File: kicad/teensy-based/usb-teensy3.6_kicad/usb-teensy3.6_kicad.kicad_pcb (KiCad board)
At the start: 2 copper layers, 154.9 x 90.2 mm, 20 parts, among them SW1 SW_Push, SW2 SW_Push, U1 Teensy3.6

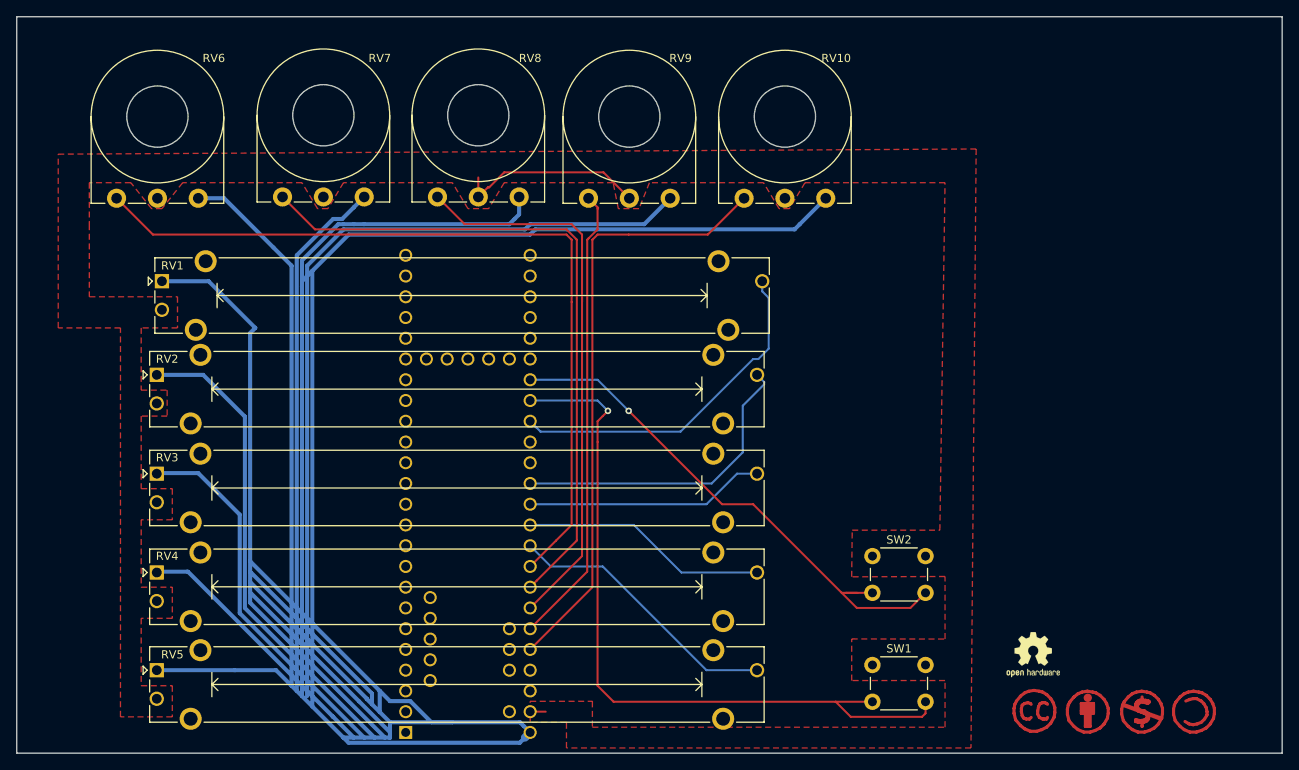
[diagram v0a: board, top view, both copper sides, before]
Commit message: modifies the soilmask and printing to underline the community thing a bit more
adds scheme to readme and howto order

As hint: I know you can easier order if the gerber files are already uploaded to a manufacturer, but as this is combine to the Affiliate Systems I decided not to.
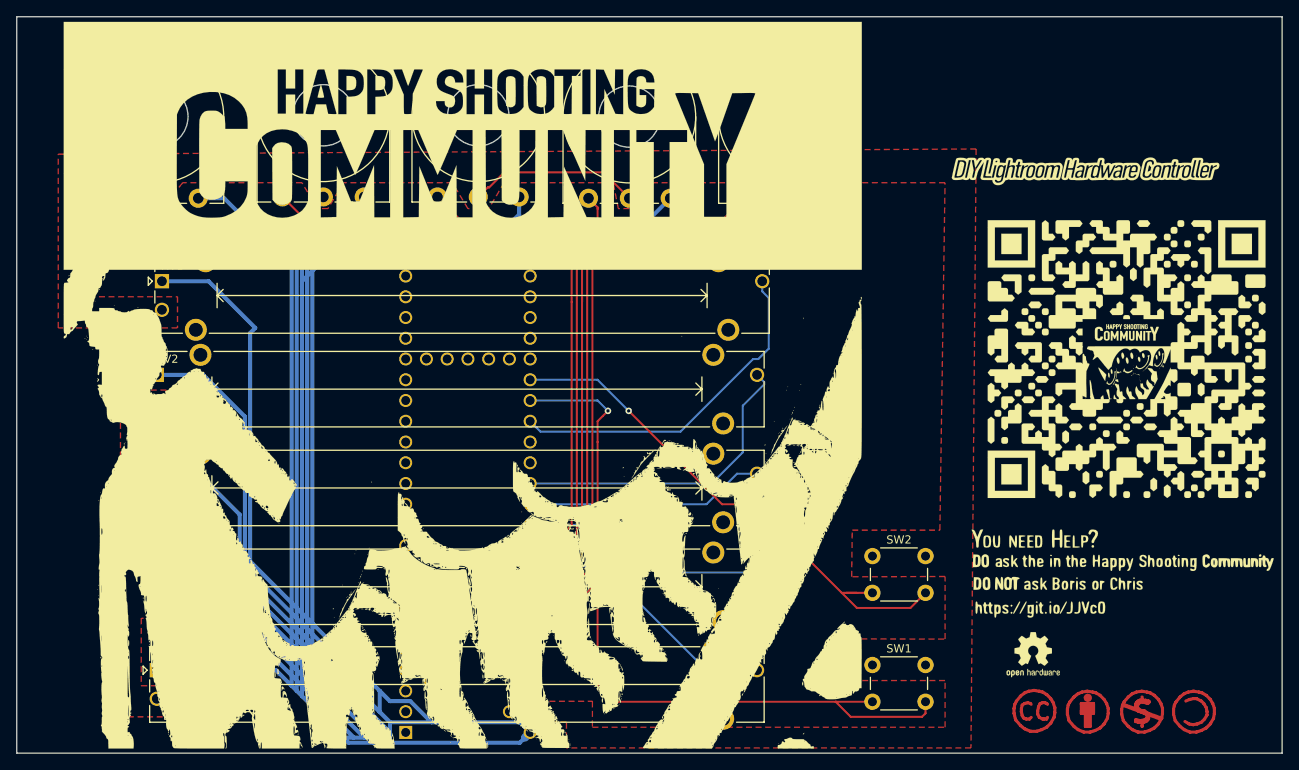
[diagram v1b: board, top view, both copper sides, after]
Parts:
- removed HSLogo: LOGO, HappyShooting:HSSilk_big
- removed HSLogoText: LOGO, HappyShooting:hsc_pcb_text_small
- added G***: LOGO, HappyShooting:hct_diff_print_i, F.Cu at (128.3, 104.8)
- added G***: LOGO, HappyShooting:diy_silk_i, F.Cu at (203.8, 78.1)
- added G***: LOGO, HappyShooting:diy_print, F.Cu at (203.8, 78.1)
- added G***: LOGO, HappyShooting:help_print, F.Cu at (209.6, 127.6)
- added G***: LOGO, HappyShooting:qr_medium, F.Cu at (209.6, 101.6)
- added G***: LOGO, HappyShooting:hct_silk_i, F.Cu at (128.3, 104.8)

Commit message: changed help wording on pcb and scheme
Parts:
- removed the G*** at (209.6, 127.6)
- added G***: LOGO, HappyShooting:help_print_350, F.Cu at (210.2, 127.6)
- moved G*** 0.64 mm to (127.6, 104.8)

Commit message: mod render without parts
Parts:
- removed the G*** at (128.3, 104.8)
- removed the G*** at (127.6, 104.8)
- removed RV1: 10k sl, Potentiometer_THT:Potentiometer_Bourns_PTA6043_Single_Slide
- added G***: LOGO, HappyShooting:hsc_diff_print_i_375, F.Cu at (130.8, 104.8)
- added G***: LOGO, HappyShooting:hsc_silk_375, F.Cu at (130.8, 104.8)

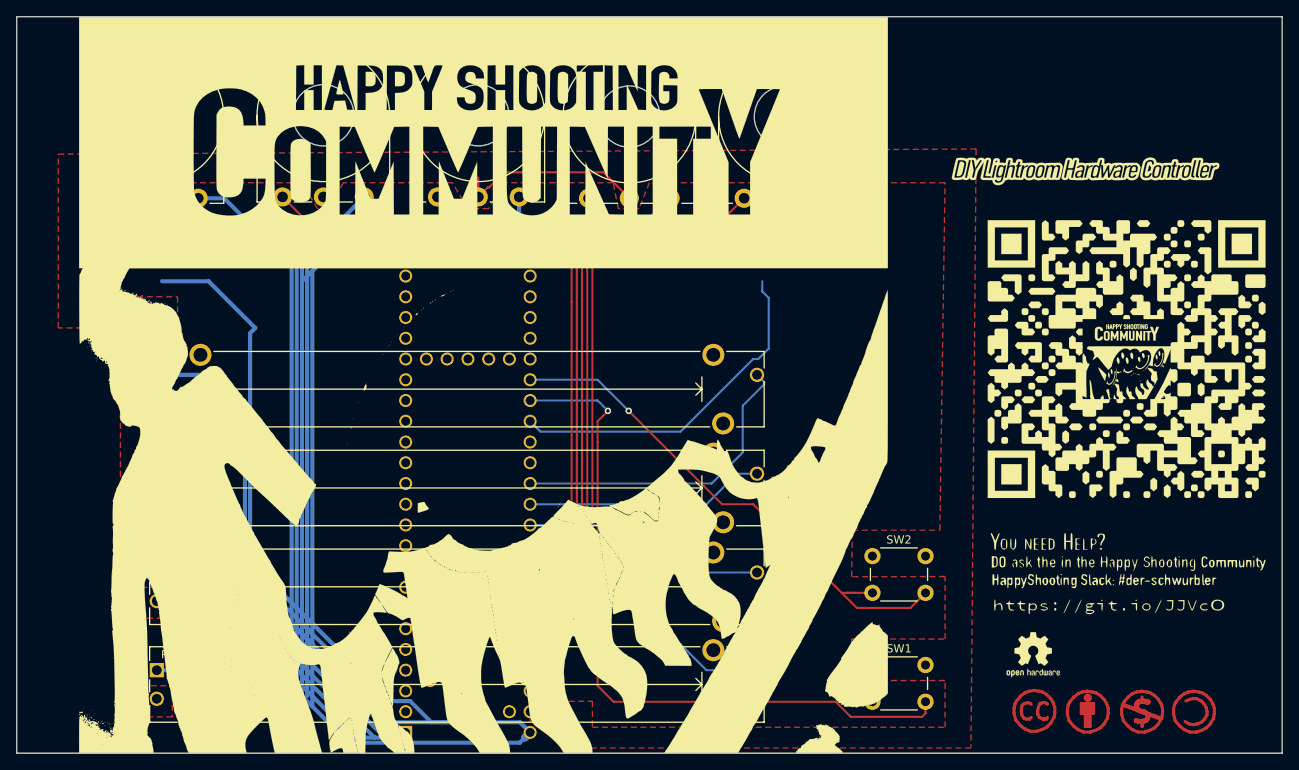
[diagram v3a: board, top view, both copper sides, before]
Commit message: update pcb with alternative layout
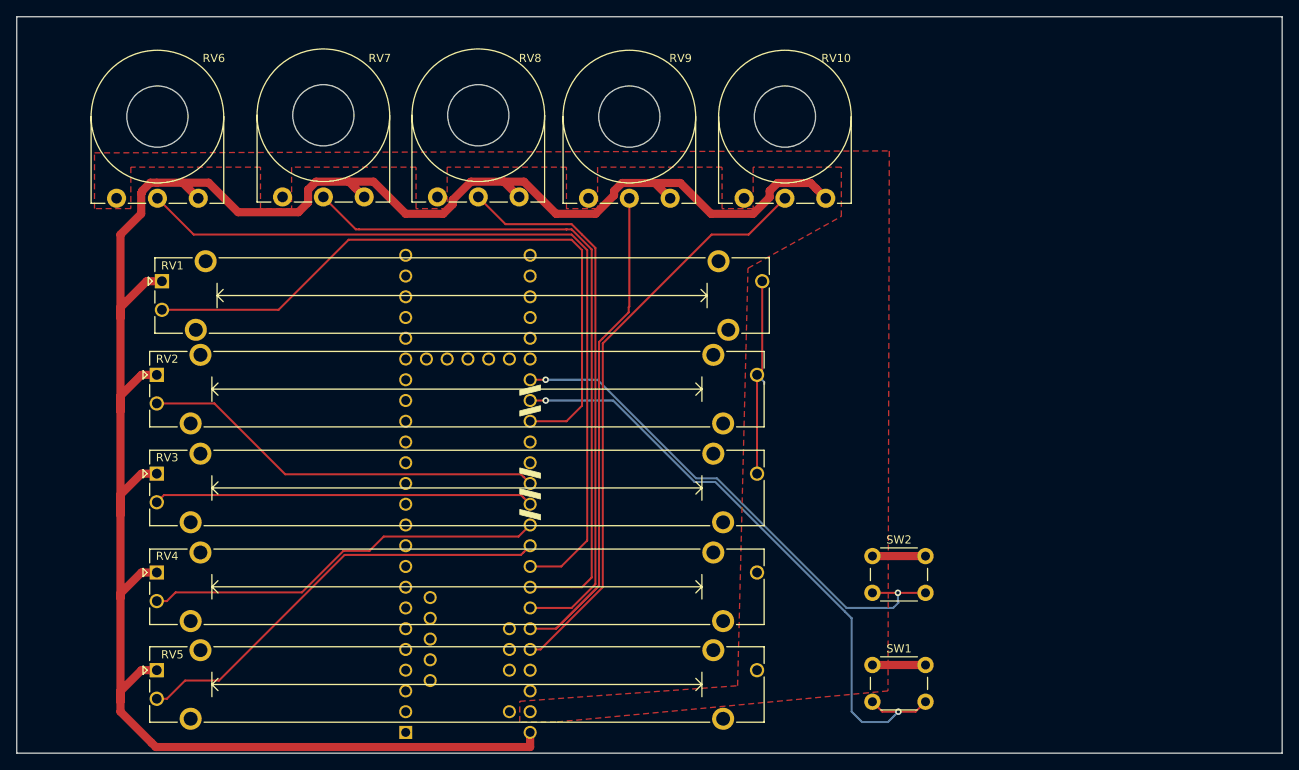
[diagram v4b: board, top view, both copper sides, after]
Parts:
- removed G***: LOGO, HappyShooting:hsc_diff_print_i_375
- removed G***: LOGO, HappyShooting:hsc_silk_375
- removed G***: LOGO, HappyShooting:help_print_350
- removed G***: LOGO, HappyShooting:diy_silk_i
- removed G***: LOGO, HappyShooting:diy_print
- removed G***: LOGO, HappyShooting:qr_medium
- removed REF**: Symbol_CC-ShareAlike_CopperTop_Small, Symbol:Symbol_CC-ShareAlike_CopperTop_Small
- removed REF**: Symbol_CreativeCommons_CopperTop_Type2_Small, Symbol:Symbol_CreativeCommons_CopperTop_Type2_Small
- removed REF**: OSHW-Logo2_7.3x6mm_SilkScreen, Symbol:OSHW-Logo2_7.3x6mm_SilkScreen
- removed REF**: Symbol_CC-Attribution_CopperTop_Small, Symbol:Symbol_CC-Attribution_CopperTop_Small
- removed REF**: Symbol_CC-Noncommercial_CopperTop_Small, Symbol:Symbol_CC-Noncommercial_CopperTop_Small
- added RV1: 10k sl, Potentiometer_THT:Potentiometer_Bourns_PTA6043_Single_Slide, F.Cu at (91.4, 92.1)
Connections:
- RV10 pad 2: GND -> Net-(RV10-Pad2)
- RV10 pad 3: Net-(RV10-Pad3) -> GND
- RV2 pad 2: GND -> Net-(RV2-Pad2)
- RV2 pad 3: Net-(RV2-Pad3) -> GND
- RV3 pad 2: GND -> Net-(RV3-Pad2)
- RV3 pad 3: Net-(RV3-Pad3) -> GND
- RV4 pad 2: GND -> Net-(RV4-Pad2)
- RV4 pad 3: Net-(RV4-Pad3) -> GND
- RV5 pad 2: GND -> Net-(RV5-Pad2)
- RV5 pad 3: Net-(RV5-Pad3) -> GND
- RV6 pad 2: GND -> Net-(RV6-Pad2)
- RV6 pad 3: Net-(RV6-Pad3) -> GND
- RV7 pad 2: GND -> Net-(RV7-Pad2)
- RV7 pad 3: Net-(RV7-Pad3) -> GND
- RV8 pad 2: GND -> Net-(RV8-Pad2)
- RV8 pad 3: Net-(RV8-Pad3) -> GND
- RV9 pad 2: GND -> Net-(RV9-Pad2)
- RV9 pad 3: Net-(RV9-Pad3) -> GND
- U1 pad 41: Net-(RV2-Pad3) -> Net-(RV2-Pad2)
- U1 pad 42: Net-(RV3-Pad3) -> Net-(RV3-Pad2)
- U1 pad 43: Net-(RV4-Pad3) -> Net-(RV4-Pad2)
- U1 pad 44: Net-(RV5-Pad3) -> Net-(RV5-Pad2)
- U1 pad 45: Net-(RV6-Pad3) -> Net-(RV6-Pad2)
- U1 pad 46: Net-(RV7-Pad3) -> Net-(RV7-Pad2)
- U1 pad 47: Net-(RV8-Pad3) -> Net-(RV8-Pad2)
- U1 pad 48: Net-(RV9-Pad3) -> Net-(RV9-Pad2)
- U1 pad 49: Net-(RV10-Pad3) -> Net-(RV10-Pad2)
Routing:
- net Net-(RV1-Pad1): track 837.6 -> 264.5 mm
- net Net-(RV6-Pad3): track 99.9 -> 0.00 mm
- net Net-(RV6-Pad2): track 0.00 -> 99.1 mm
- net Net-(RV7-Pad2): track 0.00 -> 83.7 mm
- net Net-(RV7-Pad3): track 83.1 -> 0.00 mm
- net Net-(RV10-Pad3): track 74.0 -> 0.00 mm
- net Net-(RV10-Pad2): track 0.00 -> 71.6 mm
- net Net-(RV8-Pad3): track 68.6 -> 0.00 mm
- net Net-(RV8-Pad2): track 0.00 -> 67.3 mm
- net Net-(RV9-Pad2): track 0.00 -> 67.0 mm
- net Net-(RV9-Pad3): track 56.6 -> 0.00 mm
- net Net-(RV5-Pad2): track 0.00 -> 53.5 mm
- net Net-(RV4-Pad2): track 0.00 -> 50.2 mm
- net Net-(RV2-Pad2): track 0.00 -> 49.8 mm
- net Net-(RV3-Pad2): track 0.00 -> 46.6 mm
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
